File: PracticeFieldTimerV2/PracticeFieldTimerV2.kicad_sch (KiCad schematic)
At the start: 22 parts, among them J1 External Controls, J2 Screw_Terminal_01x04, J3 Panel, J5 /CAN Enable, J6 RJ45-B, J7 RJ45-A, U1 ESP32-DevKitC

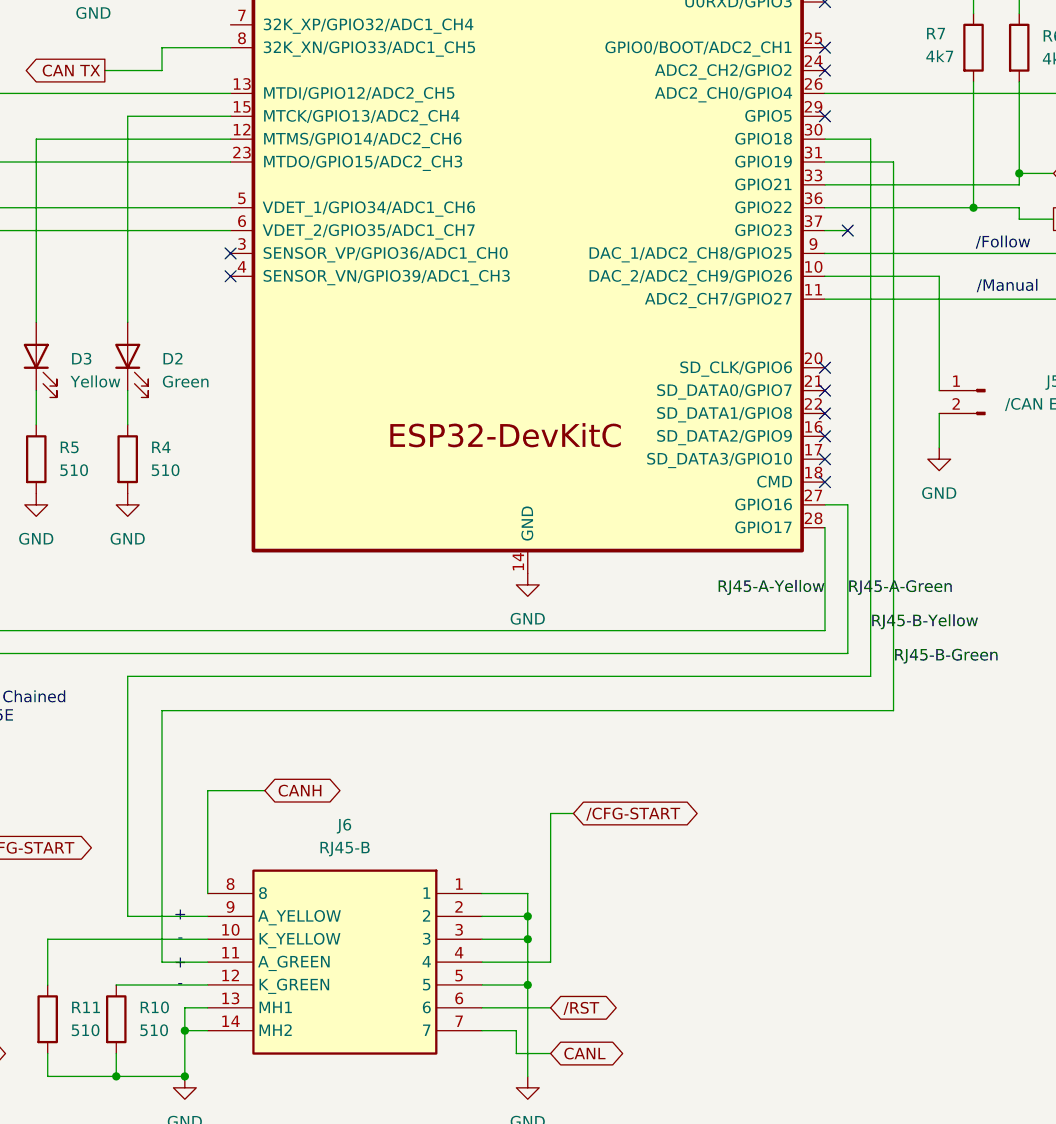
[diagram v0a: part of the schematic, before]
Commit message: Add jumper pins to control CAN bus termination. Counters at the end of the CAN bus MUST connect the pins. Others MUST leave the pins disconnected.
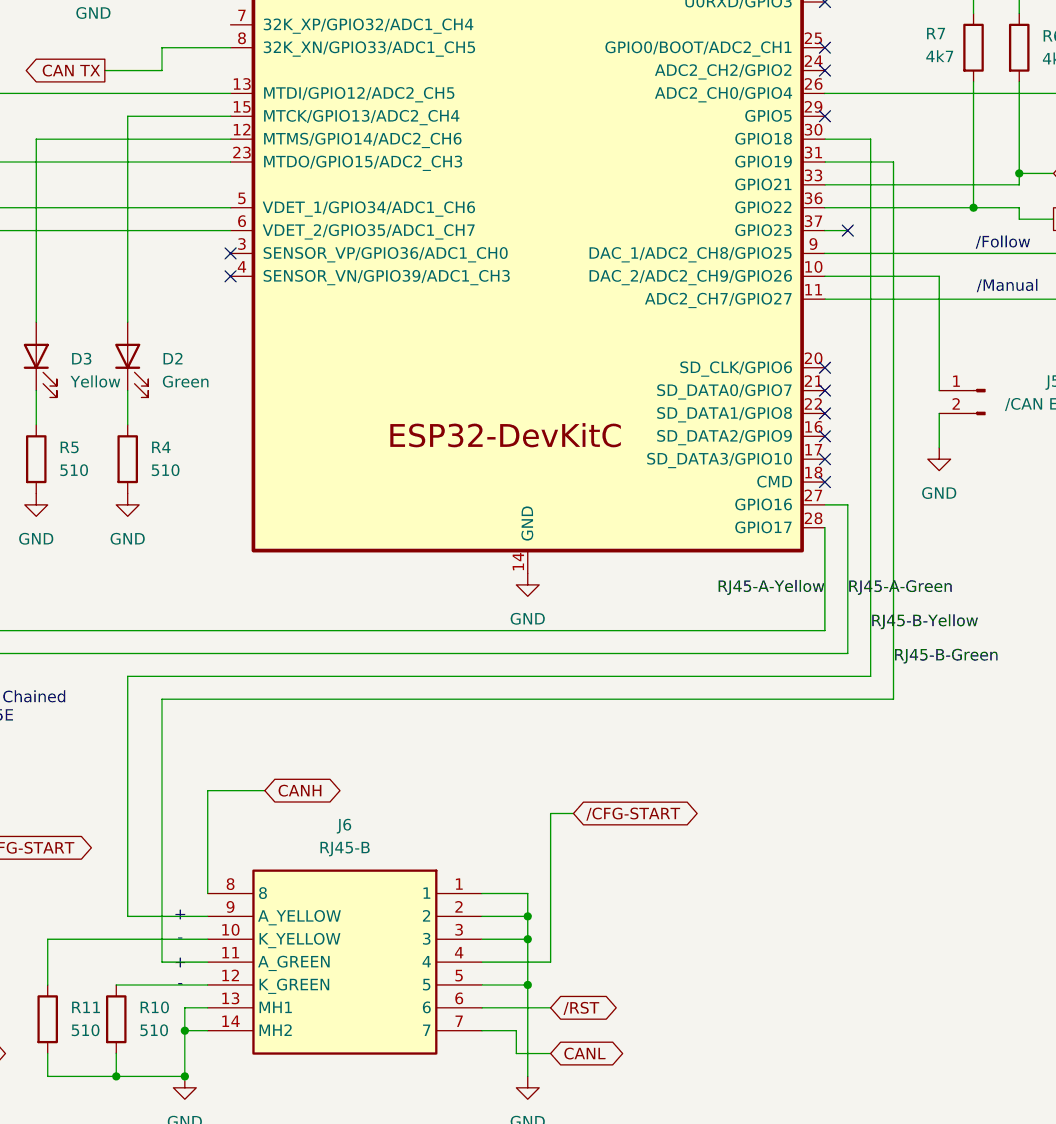
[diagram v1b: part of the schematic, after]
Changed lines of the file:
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@@
 	(wire
 		(pts
-			(xy 176.53 156.21) (xy 95.25 156.21)
+			(xy 176.53 154.94) (xy 95.25 154.94)
 		)
 		(stroke
@@
 	(wire
 		(pts
-			(xy 176.53 95.25) (xy 176.53 156.21)
+			(xy 176.53 95.25) (xy 176.53 154.94)
 		)
 		(stroke
@@
 	(wire
 		(pts
-			(xy 95.25 156.21) (xy 95.25 184.15)
-		)
-		(stroke
+			(xy 95.25 154.94) (xy 95.25 184.15)
+		)
+		(stroke
